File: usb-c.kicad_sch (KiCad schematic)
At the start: 16 parts, among them IC1 USBLC6-2SC6, IC2 632723100011, IC3 TCPP01-M12, Q1 STL11N3LLH6

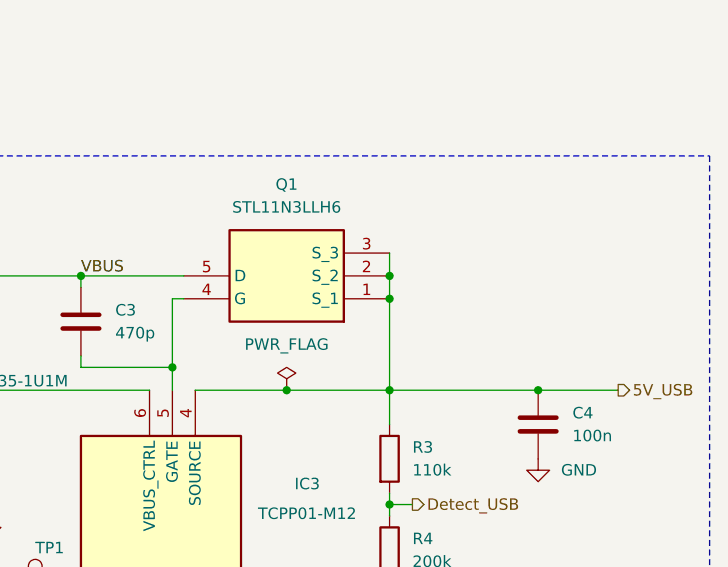
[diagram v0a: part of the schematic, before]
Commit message: Fiw warnings concerning multiple name for the same label
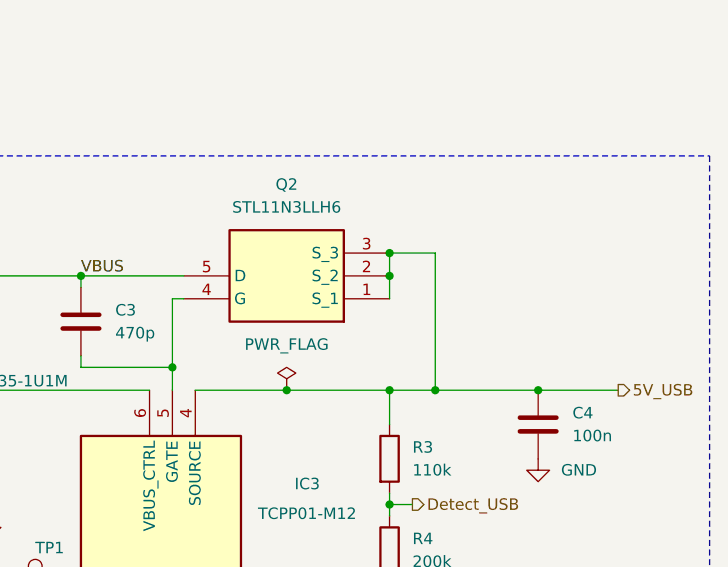
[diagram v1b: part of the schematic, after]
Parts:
- removed Q1: STL11N3LLH6, weather-station-poc-fp:STL20N6F7, symbol weather-station-poc-sym:STL11N3LLH6
- added Q2: STL11N3LLH6, weather-station-poc-fp:STL20N6F7, symbol weather-station-poc-sym:STL11N3LLH6
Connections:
- net 5V_USB: now also Q2.1 (S_1), Q2.2 (S_2), Q2.3 (S_3)
- net VBUS: now also Q2.5 (D)
- net at C3.2, IC3.5 (GATE): now also Q2.4 (G)
